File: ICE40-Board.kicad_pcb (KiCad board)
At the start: 4 copper layers, 85 parts, among them Q1 2N222, U1 ICE40HX4K-TQ144

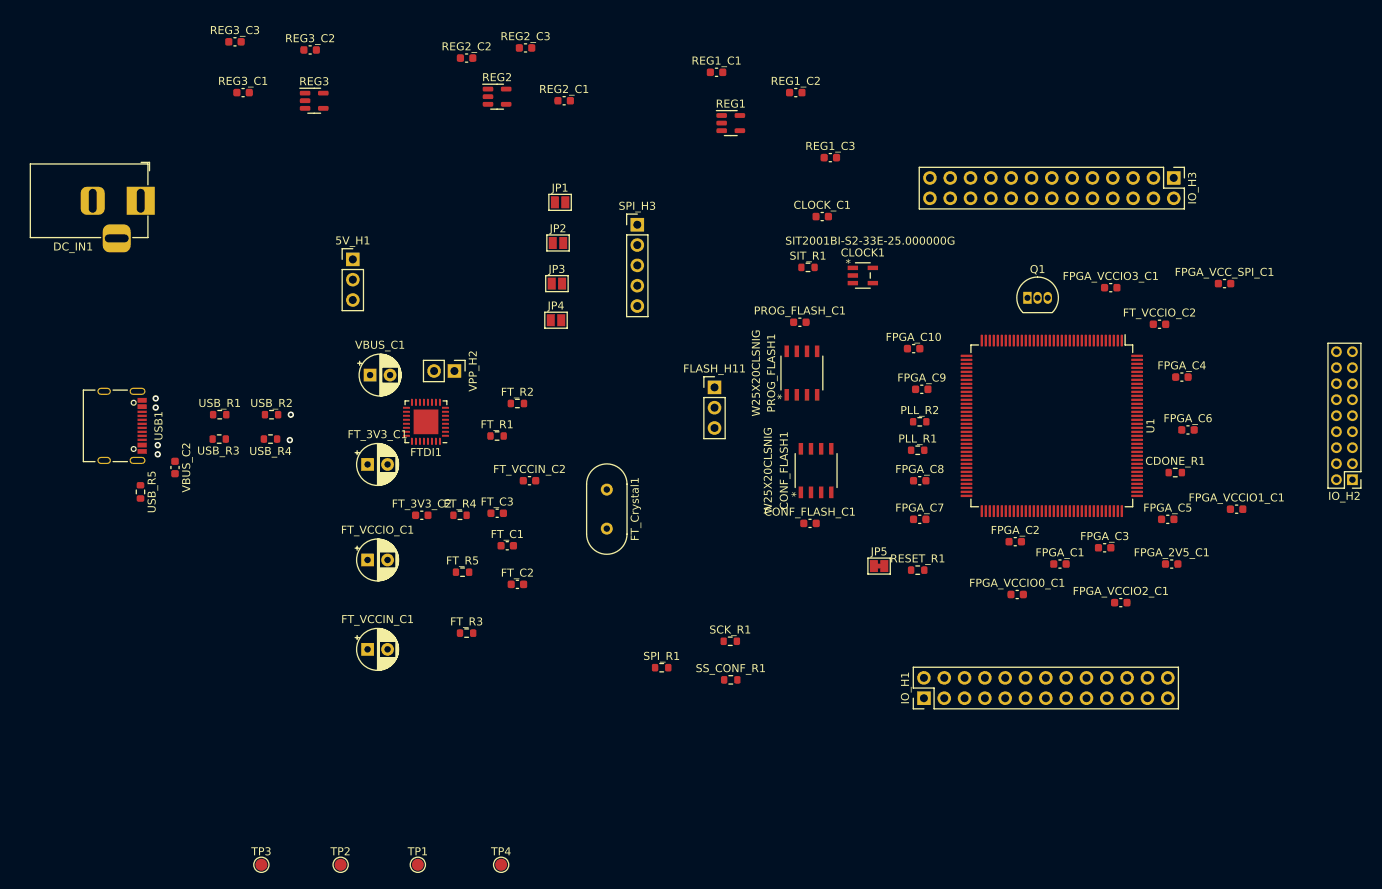
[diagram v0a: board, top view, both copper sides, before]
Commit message: Begun initial routing with simple reference designation
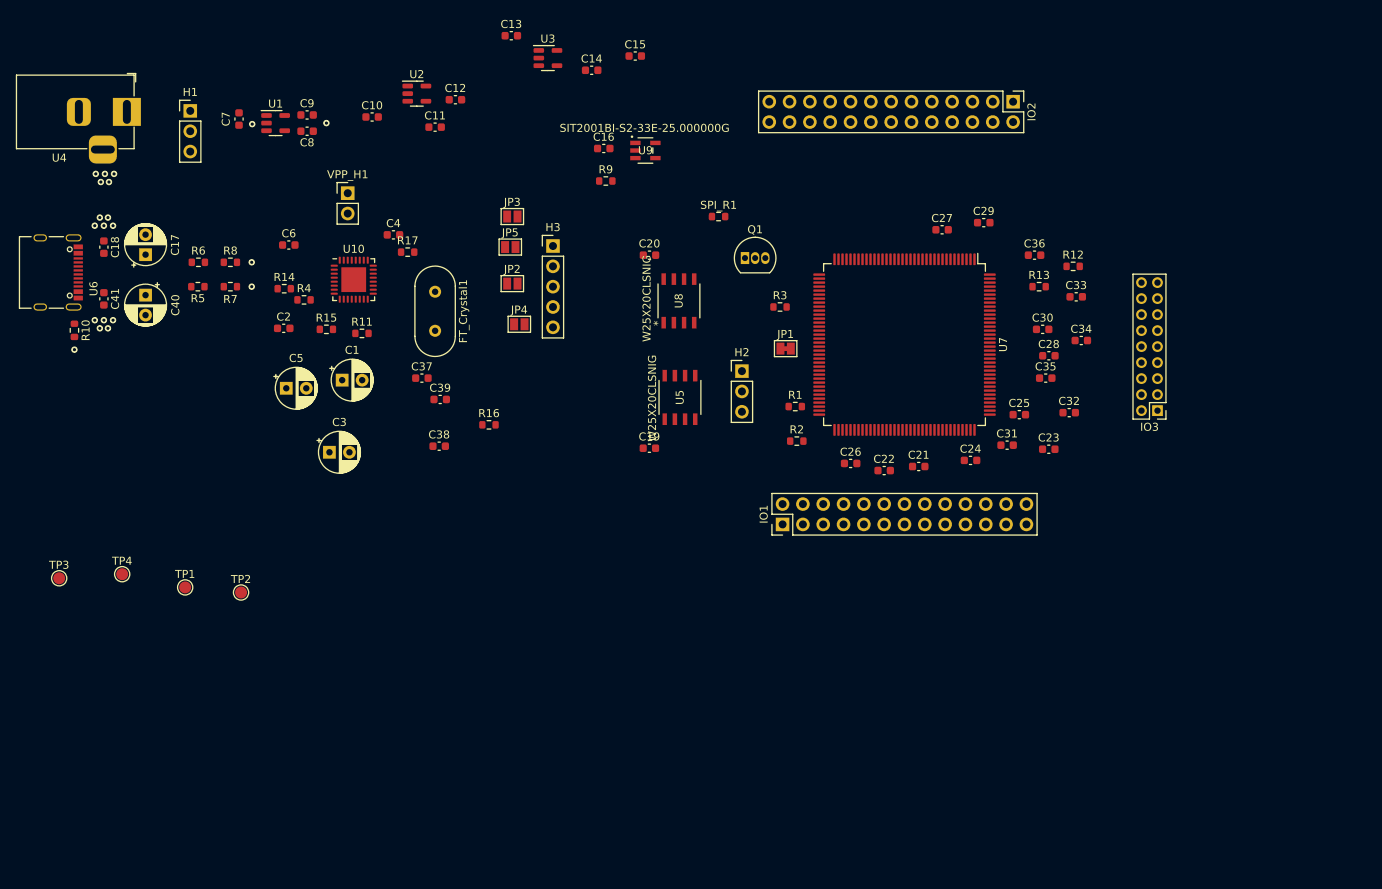
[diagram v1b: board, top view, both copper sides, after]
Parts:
- removed 5V_H1, FLASH_H11: Conn_01x03, Connector_PinHeader_2.54mm:PinHeader_1x03_P2.54mm_Vertical
- removed CDONE_R1: R, Resistor_SMD:R_0603_1608Metric
- removed CLOCK1: SIT2001BI-S2-33E-25.000000G, SIT2001BC-S2-33E-25.0:SIT2001BC-S2-33E-25.0
- removed CLOCK_C1, CONF_FLASH_C1, FPGA_2V5_C1, FPGA_C10, FPGA_C2, FPGA_C5, FPGA_C8, FPGA_VCCIO0_C1, FPGA_VCCIO1_C1, FPGA_VCCIO2_C1, FPGA_VCCIO3_C1, FPGA_VCC_SPI_C1, FT_3V3_C2, FT_VCCIN_C2, FT_VCCIO_C2, PROG_FLASH_C1, VBUS_C2: 0.1uF, Capacitor_SMD:C_0603_1608Metric
- removed CONF_FLASH1, PROG_FLASH1: W25X20CLSNIG, W25X20CLSNIG:W25X20CLSNIG
- removed DC_IN1: Barrel_Jack, Connector_BarrelJack:BarrelJack_Horizontal
- removed FPGA_C1, FPGA_C4: 1uF, Capacitor_SMD:C_0603_1608Metric
- removed FPGA_C3, FPGA_C6, REG1_C2, REG2_C2, REG3_C2: 10nF, Capacitor_SMD:C_0603_1608Metric
- removed FPGA_C7, FPGA_C9: 10uF, Capacitor_SMD:C_0603_1608Metric
- removed FTDI1: FT4222HQ, Package_DFN_QFN:VQFN-32-1EP_5x5mm_P0.5mm_EP3.1x3.1mm
- removed FT_3V3_C1, FT_VCCIN_C1, FT_VCCIO_C1, VBUS_C1: 4.7uF, Capacitor_THT:CP_Radial_D5.0mm_P2.50mm
- removed FT_C1, FT_C2, FT_C3: 27pF, Capacitor_SMD:C_0603_1608Metric
- removed FT_R1, USB_R5: 1M, Resistor_SMD:R_0603_1608Metric
- removed FT_R2: 12k, Resistor_SMD:R_0603_1608Metric
- removed FT_R3: 47k, Resistor_SMD:R_0603_1608Metric
- removed FT_R4, RESET_R1, SCK_R1, SS_CONF_R1: 10k, Resistor_SMD:R_0603_1608Metric
- removed FT_R5, SIT_R1: 1k, Resistor_SMD:R_0603_1608Metric
- removed IO_H1, IO_H3: Conn_02x13_Row_Letter_Last, Connector_PinHeader_2.54mm:PinHeader_2x13_P2.54mm_Vertical
- removed IO_H2: Conn_02x09_Row_Letter_Last, Connector_PinHeader_2.00mm:PinHeader_2x09_P2.00mm_Vertical
- removed PLL_R1, PLL_R2, USB_R2, USB_R4: 100, Resistor_SMD:R_0603_1608Metric
- removed REG1: ADP1712AUJZ-1.2, Package_TO_SOT_SMD:SOT-23-5
- removed REG1_C1, REG1_C3, REG2_C1, REG2_C3, REG3_C1, REG3_C3: 2.2uF, Capacitor_SMD:C_0603_1608Metric
- removed REG2: ADP1712AUJZ-2.5, Package_TO_SOT_SMD:SOT-23-5
- removed REG3: ADP1712AUJZ-3.3, Package_TO_SOT_SMD:SOT-23-5
- removed SPI_H3: Conn_01x05, Connector_PinHeader_2.54mm:PinHeader_1x05_P2.54mm_Vertical
- removed USB1: USB_C_Receptacle_USB2.0, Connector_USB:USB_C_Receptacle_Palconn_UTC16-G
- removed USB_R1, USB_R3: 5.1k, Resistor_SMD:R_0603_1608Metric
- removed VPP_H2: Conn_01x02, Connector_PinHeader_2.54mm:PinHeader_1x02_P2.54mm_Vertical
- added C1: 4.7uF, Capacitor_THT:CP_Radial_D5.0mm_P2.50mm, F.Cu at (60.9, 58.3)
- added C10: 2.2uF, Capacitor_SMD:C_0603_1608Metric, F.Cu at (64.6, 25.4)
- added C11: 10nF, Capacitor_SMD:C_0603_1608Metric, F.Cu at (72.5, 26.7)
- added C12: 2.2uF, Capacitor_SMD:C_0603_1608Metric, F.Cu at (75.1, 23.2)
- added C13: 2.2uF, Capacitor_SMD:C_0603_1608Metric, F.Cu at (82.0, 15.2)
- added C14: 10nF, Capacitor_SMD:C_0603_1608Metric, F.Cu at (92.1, 19.6)
- added C15: 2.2uF, Capacitor_SMD:C_0603_1608Metric, F.Cu at (97.5, 17.8)
- added C16: 0.1uF, Capacitor_SMD:C_0603_1608Metric, F.Cu at (93.6, 29.3)
- added C17: 4.7uF, Capacitor_THT:CP_Radial_D5.0mm_P2.50mm, F.Cu at (36.3, 42.6)
- added C18: 0.1uF, Capacitor_SMD:C_0603_1608Metric, F.Cu at (31.1, 41.7)
- added C19: 0.1uF, Capacitor_SMD:C_0603_1608Metric, F.Cu at (99.3, 66.8)
- added C2: 0.1uF, Capacitor_SMD:C_0603_1608Metric, F.Cu at (53.6, 51.8)
- added C20: 0.1uF, Capacitor_SMD:C_0603_1608Metric, F.Cu at (99.3, 42.7)
- added C21: 0.1uF, Capacitor_SMD:C_0603_1608Metric, F.Cu at (133.0, 69.1)
- added C22: 0.1uF, Capacitor_SMD:C_0603_1608Metric, F.Cu at (128.7, 69.6)
- added C23: 0.1uF, Capacitor_SMD:C_0603_1608Metric, F.Cu at (149.2, 66.9)
- added C24: 0.1uF, Capacitor_SMD:C_0603_1608Metric, F.Cu at (139.4, 68.3)
- added C25: 0.1uF, Capacitor_SMD:C_0603_1608Metric, F.Cu at (145.5, 62.6)
- added C26: 0.1uF, Capacitor_SMD:C_0603_1608Metric, F.Cu at (124.5, 68.7)
- added C27: 1uF, Capacitor_SMD:C_0603_1608Metric, F.Cu at (135.9, 39.5)
- added C28: 0.1uF, Capacitor_SMD:C_0603_1608Metric, F.Cu at (149.2, 55.2)
- added C29: 10nF, Capacitor_SMD:C_0603_1608Metric, F.Cu at (141.1, 38.6)
- added C3: 4.7uF, Capacitor_THT:CP_Radial_D5.0mm_P2.50mm, F.Cu at (59.3, 67.3)
- added C30: 1uF, Capacitor_SMD:C_0603_1608Metric, F.Cu at (148.5, 51.9)
- added C31: 0.1uF, Capacitor_SMD:C_0603_1608Metric, F.Cu at (144.0, 66.4)
- added C32: 10nF, Capacitor_SMD:C_0603_1608Metric, F.Cu at (151.8, 62.4)
- added C33: 10uF, Capacitor_SMD:C_0603_1608Metric, F.Cu at (152.7, 47.9)
- added C34: 0.1uF, Capacitor_SMD:C_0603_1608Metric, F.Cu at (153.3, 53.3)
- added C35: 10uF, Capacitor_SMD:C_0603_1608Metric, F.Cu at (148.8, 58.0)
- added C36: 0.1uF, Capacitor_SMD:C_0603_1608Metric, F.Cu at (147.4, 42.7)
- added C37: 27pF, Capacitor_SMD:C_0603_1608Metric, F.Cu at (70.9, 58.0)
- added C38: 27pF, Capacitor_SMD:C_0603_1608Metric, F.Cu at (73.0, 66.5)
- added C39: 27pF, Capacitor_SMD:C_0603_1608Metric, F.Cu at (73.2, 60.7)
- added C4: 0.1uF, Capacitor_SMD:C_0603_1608Metric, F.Cu at (67.3, 40.1)
- added C40: 4.7uF, Capacitor_THT:CP_Radial_D5.0mm_P2.50mm, F.Cu at (36.3, 47.7)
- added C41: 0.1uF, Capacitor_SMD:C_0603_1608Metric, F.Cu at (31.1, 48.1)
- added C5: 4.7uF, Capacitor_THT:CP_Radial_D5.0mm_P2.50mm, F.Cu at (53.9, 59.3)
- added C6: 0.1uF, Capacitor_SMD:C_0603_1608Metric, F.Cu at (54.2, 41.4)
- added C7: 2.2uF, Capacitor_SMD:C_0603_1608Metric, F.Cu at (48.0, 25.7)
- added C8: 10nF, Capacitor_SMD:C_0603_1608Metric, F.Cu at (56.5, 27.2)
- added C9: 2.2uF, Capacitor_SMD:C_0603_1608Metric, F.Cu at (56.5, 25.1)
- added H1: Conn_01x03, Connector_PinHeader_2.54mm:PinHeader_1x03_P2.54mm_Vertical, F.Cu at (41.9, 24.6)
- added H2: Conn_01x03, Connector_PinHeader_2.54mm:PinHeader_1x03_P2.54mm_Vertical, F.Cu at (110.9, 57.2)
- added H3: Conn_01x05, Connector_PinHeader_2.54mm:PinHeader_1x05_P2.54mm_Vertical, F.Cu at (87.2, 41.5)
- added IO1: Conn_02x13_Row_Letter_Last, Connector_PinHeader_2.54mm:PinHeader_2x13_P2.54mm_Vertical, F.Cu at (116.0, 76.3)
- added IO2: Conn_02x13_Row_Letter_Last, Connector_PinHeader_2.54mm:PinHeader_2x13_P2.54mm_Vertical, F.Cu at (144.8, 23.5)
- added IO3: Conn_02x09_Row_Letter_Last, Connector_PinHeader_2.00mm:PinHeader_2x09_P2.00mm_Vertical, F.Cu at (162.8, 62.1)
- added R1: 10k, Resistor_SMD:R_0603_1608Metric, F.Cu at (117.5, 61.6)
- added R10: 1M, Resistor_SMD:R_0603_1608Metric, F.Cu at (27.4, 52.1)
- added R11: 1k, Resistor_SMD:R_0603_1608Metric, F.Cu at (63.4, 52.5)
- added R12: 100, Resistor_SMD:R_0603_1608Metric, F.Cu at (152.3, 44.1)
- added R13: 100, Resistor_SMD:R_0603_1608Metric, F.Cu at (148.0, 46.6)
- added R14: 47k, Resistor_SMD:R_0603_1608Metric, F.Cu at (53.7, 46.9)
- added R15: 10k, Resistor_SMD:R_0603_1608Metric, F.Cu at (58.9, 51.9)
- added R16: 1M, Resistor_SMD:R_0603_1608Metric, F.Cu at (79.2, 63.9)
- added R17: 12k, Resistor_SMD:R_0603_1608Metric, F.Cu at (69.1, 42.3)
- added R2: 10k, Resistor_SMD:R_0603_1608Metric, F.Cu at (117.7, 65.9)
- added R3: R, Resistor_SMD:R_0603_1608Metric, F.Cu at (115.6, 49.1)
- added R4: 10k, Resistor_SMD:R_0603_1608Metric, F.Cu at (56.1, 48.3)
- added R5: 5.1k, Resistor_SMD:R_0603_1608Metric, F.Cu at (42.9, 46.6)
- added R6: 5.1k, Resistor_SMD:R_0603_1608Metric, F.Cu at (42.9, 43.6)
- added R7: 100, Resistor_SMD:R_0603_1608Metric, F.Cu at (46.9, 46.6)
- added R8: 100, Resistor_SMD:R_0603_1608Metric, F.Cu at (46.9, 43.6)
- added R9: 1k, Resistor_SMD:R_0603_1608Metric, F.Cu at (93.9, 33.4)
- added U10: FT4222HQ, Package_DFN_QFN:VQFN-32-1EP_5x5mm_P0.5mm_EP3.1x3.1mm, F.Cu at (62.3, 45.7)
- added U2: ADP1712AUJZ-2.5, Package_TO_SOT_SMD:SOT-23-5, F.Cu at (70.2, 22.5)
- added U3: ADP1712AUJZ-1.2, Package_TO_SOT_SMD:SOT-23-5, F.Cu at (86.6, 18.0)
- added U4: Barrel_Jack, Connector_BarrelJack:BarrelJack_Horizontal, F.Cu at (34.0, 24.8)
- added U5: W25X20CLSNIG, W25X20CLSNIG:W25X20CLSNIG, F.Cu at (103.1, 60.5)
- added U6: USB_C_Receptacle_USB2.0, Connector_USB:USB_C_Receptacle_Palconn_UTC16-G, F.Cu at (25.4, 44.8)
- added U7: ICE40HX4K-TQ144, Package_QFP:TQFP-144_20x20mm_P0.5mm, F.Cu at (131.2, 53.8)
- added U8: W25X20CLSNIG, W25X20CLSNIG:W25X20CLSNIG, F.Cu at (103.0, 48.4)
- added U9: SIT2001BI-S2-33E-25.000000G, SIT2001BC-S2-33E-25.0:SIT2001BC-S2-33E-25.0, F.Cu at (98.8, 29.6)
- added VPP_H1: Conn_01x02, Connector_PinHeader_2.54mm:PinHeader_1x02_P2.54mm_Vertical, F.Cu at (61.6, 34.9)
- JP1: value SCK -> SolderJumper_2_Bridged; footprint Jumper:SolderJumper-2_P1.3mm_Open_Pad1.0x1.5mm -> Jumper:SolderJumper-2_P1.3mm_Bridged_Pad1.0x1.5mm
- JP2: value MOSI -> SCK
- JP3: value MISO -> MOSI
- JP4: value SS -> MISO
- JP5: value SolderJumper_2_Bridged -> SS; footprint Jumper:SolderJumper-2_P1.3mm_Bridged_Pad1.0x1.5mm -> Jumper:SolderJumper-2_P1.3mm_Open_Pad1.0x1.5mm
- U1: value ICE40HX4K-TQ144 -> ADP1712AUJZ-3.3; footprint Package_QFP:TQFP-144_20x20mm_P0.5mm -> Package_TO_SOT_SMD:SOT-23-5
- moved U1 104.1 mm to (52.6, 26.2), turned to 0 degrees
- moved JP5 61.0 mm to (81.9, 41.7)
- moved TP4 59.7 mm to (33.4, 82.5)
- moved SPI_R1 56.8 mm to (108.0, 37.8)
- moved TP1 45.3 mm to (41.3, 84.2)
- moved TP3 43.8 mm to (25.5, 83.1)
- moved TP2 36.2 mm to (48.3, 84.8)
- moved Q1 35.7 mm to (111.3, 43.0)
- moved JP1 33.6 mm to (116.3, 54.4)
- moved FT_Crystal1 32.7 mm to (72.5, 47.2)
- moved JP3 10.1 mm to (82.2, 37.8)
- moved JP2 7.65 mm to (82.2, 46.2)
- moved JP4 4.62 mm to (83.0, 51.3)
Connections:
- JP1 pad 1: Net-(FTDI1-Pad8) -> +3V3
- JP1 pad 2: /SCK -> Net-(JP1-Pad2)
- JP2 pad 2: /MOSI -> /SCK
- JP3 pad 2: /MISO -> /MOSI
- JP4 pad 2: /SS -> /MISO
- JP5 pad 1: +3V3 -> Net-(JP5-Pad1)
- JP5 pad 2: Net-(JP5-Pad2) -> /SS
- U1 pad 1: unconnected-(U1-Pad1) -> +5V
- U1 pad 2: unconnected-(U1-Pad2) -> GND
- U1 pad 3: unconnected-(U1-Pad3) -> +5V
- U1 pad 4: unconnected-(U1-Pad4) -> Net-(C8-Pad1)
- U1 pad 5: Net-(Q1-Pad3) -> +3V3
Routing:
- net (no net): vias 6 -> 20

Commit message: Committing before changing footprints to hand solder version for resistors and capacitors
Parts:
- C1, C17, C3, C40, C5: footprint Capacitor_THT:CP_Radial_D5.0mm_P2.50mm -> Capacitor_THT:CP_Radial_D4.0mm_P2.00mm
- U4: footprint Connector_BarrelJack:BarrelJack_Horizontal -> CUI_PJ-007:CUI_PJ-007
- moved R4 71.6 mm to (127.0, 38.1), turned to 90 degrees
- moved C38 42.0 mm to (45.2, 35.0), turned to -90 degrees
- moved R16 35.8 mm to (53.8, 38.6)
- moved C39 28.9 mm to (61.5, 34.3), turned to -90 degrees
- moved C3 25.4 mm to (68.6, 43.7), turned to 90 degrees
- moved FT_Crystal1 25.0 mm to (51.1, 34.3), turned to 0 degrees
- moved R17 22.2 mm to (47.0, 39.9)
- moved C15 21.6 mm to (77.2, 25.1), turned to -90 degrees
- moved C14 21.0 mm to (72.9, 27.9), turned to 180 degrees
- moved JP4 20.2 mm to (75.0, 32.8)
- moved R14 19.8 mm to (73.3, 48.8), turned to 180 degrees
- moved VPP_H1 18.9 mm to (61.2, 53.8), turned to 180 degrees
- moved U3 15.9 mm to (72.3, 25.1)
- moved JP3 15.6 mm to (66.9, 34.5)
- moved C13 15.4 mm to (68.3, 22.3)
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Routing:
- net (no net): vias 20 -> 33

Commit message: Initial routing
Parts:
- removed C1, C17, C3, C40, C5: 4.7uF, Capacitor_THT:CP_Radial_D4.0mm_P2.00mm
- removed C41: 0.1uF, Capacitor_SMD:C_0603_1608Metric
- removed JP1: SolderJumper_2_Bridged, Jumper:SolderJumper-2_P1.3mm_Bridged_Pad1.0x1.5mm
- removed R13: 100, Resistor_SMD:R_0603_1608Metric
- removed TP1, TP2, TP3, TP4: TestPoint, TestPoint:TestPoint_Pad_D1.5mm
- C10, C11, C12, C13, C14, C15, C16, C18, C19, C2, C20, C21, C22, C23, C24, C25, C26, C28, C31, C33, C34, C36, C37, C38, C39, C4, C6, C7, C8, C9: footprint Capacitor_SMD:C_0603_1608Metric -> Capacitor_SMD:C_0603_1608Metric_Pad1.08x0.95mm_HandSolder
- C27, C30: value 1uF -> 0.1uF; footprint Capacitor_SMD:C_0603_1608Metric -> Capacitor_SMD:C_0603_1608Metric_Pad1.08x0.95mm_HandSolder
- C29, C32: value 10nF -> 0.1uF; footprint Capacitor_SMD:C_0603_1608Metric -> Capacitor_SMD:C_0603_1608Metric_Pad1.08x0.95mm_HandSolder
- C35: value 10uF -> 0.1uF; footprint Capacitor_SMD:C_0603_1608Metric -> Capacitor_SMD:C_0603_1608Metric_Pad1.08x0.95mm_HandSolder
- R1, R10, R11, R12, R14, R15, R16, R17, R2, R3, R4, R5, R6, R7, R8, R9, SPI_R1: footprint Resistor_SMD:R_0603_1608Metric -> Resistor_SMD:R_0603_1608Metric_Pad0.98x0.95mm_HandSolder
- moved C32 51.3 mm to (105.2, 40.9), turned to 180 degrees
- moved C28 47.4 mm to (105.2, 37.8), turned to 180 degrees
- moved C31 43.9 mm to (104.9, 46.5), turned to 180 degrees
- moved C22 41.7 mm to (112.6, 31.1), turned to 90 degrees
- moved C21 38.6 mm to (126.1, 31.1), turned to 90 degrees
- moved C30 38.2 mm to (116.5, 31.1), turned to 90 degrees
- moved C39 36.1 mm to (25.7, 29.7), turned to 0 degrees
- moved R4 34.1 mm to (100.5, 59.4), turned to -90 degrees
- moved R2 31.6 mm to (90.7, 49.5), turned to -90 degrees
- moved H2 29.1 mm to (85.3, 43.2)
- moved C29 29.0 mm to (121.0, 59.5), turned to -90 degrees
- moved C4 28.1 mm to (36.1, 45.2), turned to -90 degrees
- moved FT_Crystal1 27.0 mm to (24.9, 40.5), turned to 90 degrees
- moved C23 25.7 mm to (124.6, 59.5), turned to -90 degrees
- moved R1 23.9 mm to (94.7, 54.4), turned to -90 degrees
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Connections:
- C27 pad 1: +3V3 -> +1V2
- C28 pad 1: +3V3 -> +1V2
- C29 pad 1: +3V3 -> +1V2
- C30 pad 1: +3V3 -> +1V2
- C35 pad 1: /VCC_PLL2 -> +3V3
- C35 pad 2: /GND_PLL2 -> GND
- C36 pad 1: /VCC_PLL2 -> +3V3
- C36 pad 2: /GND_PLL2 -> GND
- H3 pad 3: /MISO -> /MOSI
- H3 pad 4: /MOSI -> /MISO
- Q1 pad 1: GND -> Net-(Q1-Pad1)
- Q1 pad 3: Net-(Q1-Pad3) -> +3V3
- R1 pad 2: Net-(JP1-Pad2) -> Net-(Q1-Pad1)
- R2 pad 2: Net-(JP1-Pad2) -> Net-(Q1-Pad1)
- U7 pad 103: Net-(Q1-Pad3) -> GND
- U7 pad 13: Net-(Q1-Pad3) -> GND
- U7 pad 132: Net-(Q1-Pad3) -> GND
- U7 pad 14: Net-(Q1-Pad3) -> GND
- U7 pad 140: Net-(Q1-Pad3) -> GND
- U7 pad 5: Net-(Q1-Pad3) -> GND
- U7 pad 53: /GND_PLL2 -> /GND_PLL1
- U7 pad 54: /VCC_PLL2 -> /VCC_PLL1
- U7 pad 59: Net-(Q1-Pad3) -> GND
- U7 pad 69: Net-(Q1-Pad3) -> GND
- U7 pad 72: Net-(JP1-Pad2) -> Net-(Q1-Pad1)
- U7 pad 86: Net-(Q1-Pad3) -> GND
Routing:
- net GND: track 0.00 -> 100.4 mm, vias 0 -> 30
- net VBUS: track 0.00 -> 36.8 mm, vias 0 -> 3
- net +3V3: track 0.00 -> 32.2 mm, vias 0 -> 6
- net D+: track 0.00 -> 31.6 mm, vias 0 -> 2
- net D-: track 0.00 -> 30.6 mm
- net +2V5: track 0.00 -> 21.3 mm
- net Net-(R6-Pad1): track 0.00 -> 19.7 mm, vias 0 -> 2
- net Net-(C38-Pad1): track 0.00 -> 19.2 mm
- net Net-(C39-Pad1): track 0.00 -> 18.6 mm
- net +5V: track 0.00 -> 17.5 mm
- net Net-(R5-Pad1): track 0.00 -> 9.60 mm
- net Net-(U10-Pad29): track 0.00 -> 9.40 mm
- net Net-(R17-Pad2): track 0.00 -> 6.66 mm
- net VDD: track 0.00 -> 5.58 mm
- net +1V2: track 0.00 -> 3.72 mm
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- added copper zone on In2.Cu, net +3V3
- added copper zone on In1.Cu, net GND
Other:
- board outline added: 142.2 x 61 mm

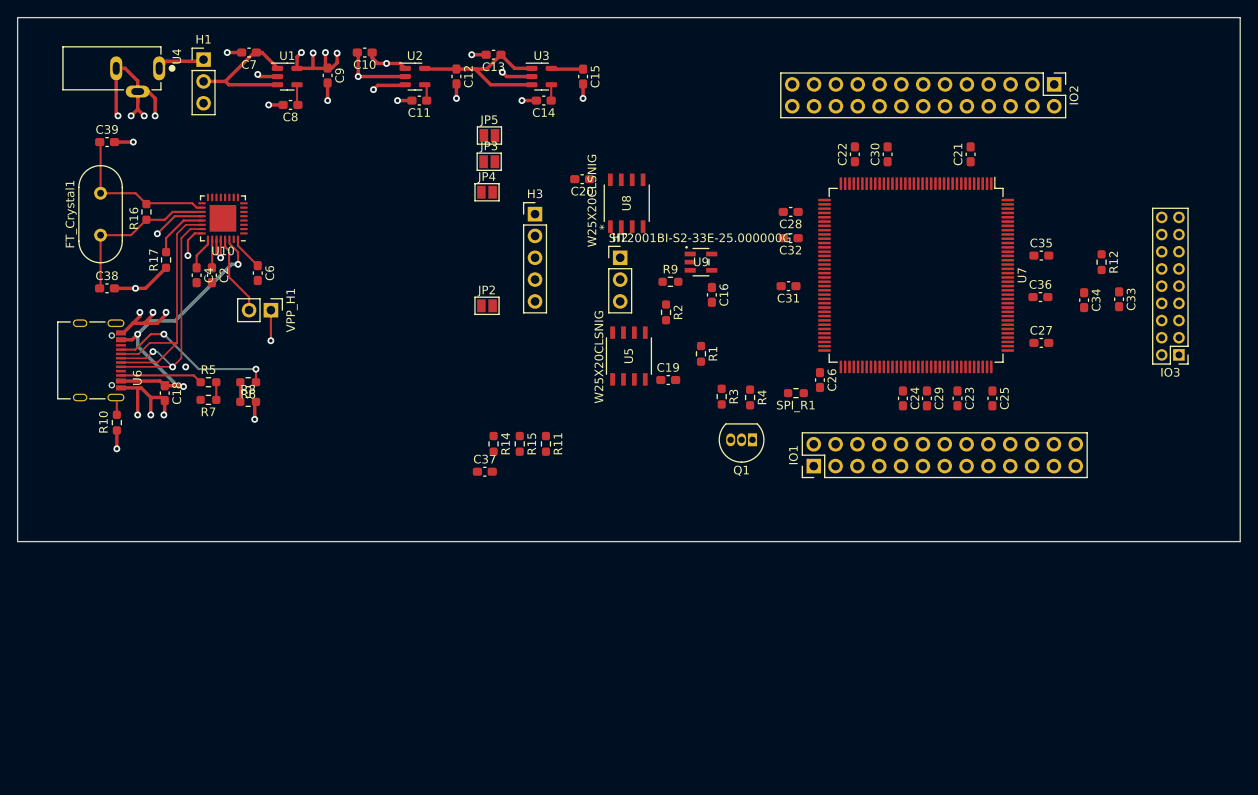
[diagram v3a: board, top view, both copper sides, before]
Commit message: USB-C routing complete
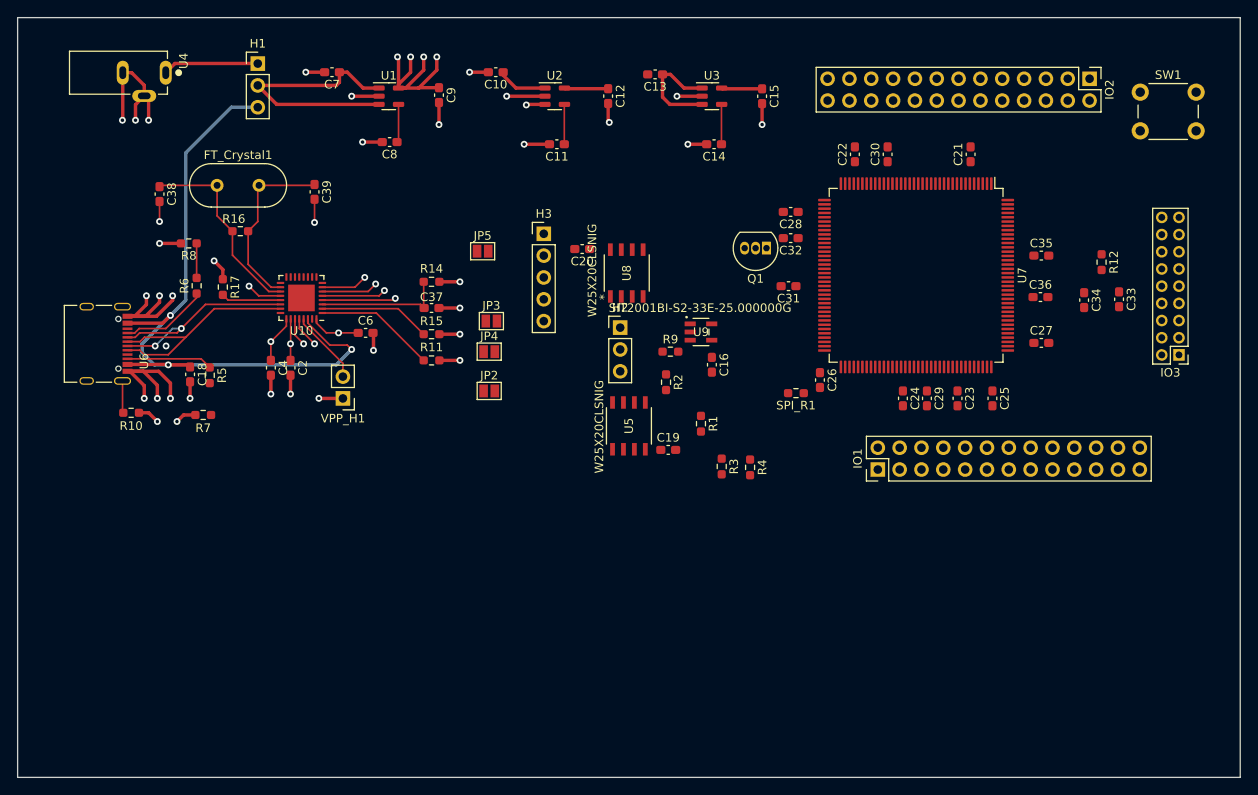
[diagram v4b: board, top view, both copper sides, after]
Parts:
- added SW1: SW_Push, Button_Switch_THT:SW_PUSH_6mm, F.Cu at (145.8, 23.9)
- moved C39 24.8 mm to (49.8, 35.5), turned to -90 degrees
- moved Q1 22.4 mm to (102.4, 42.1)
- moved C15 21.0 mm to (101.9, 24.4)
- moved C14 20.5 mm to (96.3, 30.0)
- moved R14 20.2 mm to (63.4, 46.0), turned to 180 degrees
- moved C37 20.0 mm to (63.4, 49.0), turned to 180 degrees
- moved U3 19.9 mm to (96.0, 24.4)
- moved R8 19.7 mm to (35.2, 41.5), turned to 180 degrees
- moved C13 18.9 mm to (89.4, 21.8)
- moved JP3 18.5 mm to (70.4, 50.5)
- moved JP4 18.5 mm to (70.1, 54.1)
- moved C12 17.8 mm to (83.9, 24.4)
- moved C11 16.8 mm to (78.0, 30.0)
- moved R11 16.5 mm to (63.4, 55.1), turned to 180 degrees
- moved U2 16.4 mm to (77.7, 24.4)
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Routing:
- net VBUS: track 36.8 -> 81.3 mm
- net +3V3: track 32.2 -> 74.4 mm, vias 6 -> 14
- net GND: track 100.4 -> 124.4 mm, vias 30 -> 37
- net Net-(C37-Pad2): track 0.00 -> 15.1 mm
- net Net-(R11-Pad2): track 0.00 -> 14.1 mm
- net +5V: track 17.5 -> 31.2 mm
- net Net-(R15-Pad2): track 0.00 -> 13.0 mm
- net Net-(R6-Pad1): track 19.7 -> 10.2 mm, vias 2 -> 0
- net VDD: track 5.58 -> 11.2 mm
- net D+: track 31.6 -> 27.0 mm, vias 2 -> 0
- net D-: track 30.6 -> 26.2 mm, vias 0 -> 2
- net Net-(C38-Pad1): track 19.2 -> 23.0 mm
- net +2V5: track 21.3 -> 18.0 mm
- net Net-(C14-Pad1): track 1.85 -> 4.90 mm
- net Net-(C11-Pad1): track 1.85 -> 4.65 mm
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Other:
- board size 142.2 x 61 mm -> 142.2 x 88.4 mm
